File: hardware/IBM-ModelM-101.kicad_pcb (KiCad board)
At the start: 2 copper layers, 150 x 50 mm, 44 parts, among them J1 CONN-MOLEX-0670688000-USB-B, J2 KEYBOARD_ACTIVE_LINES, J3 KEYBOARD_INPUT_LINES, J4 CHASSIS_GROUND, J5 STATUS_LEDS, J6 DEBUG_FTDI, J7 JTAG, SW1 BOOT0, SW2 RESET, U1 TLV70233DBV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

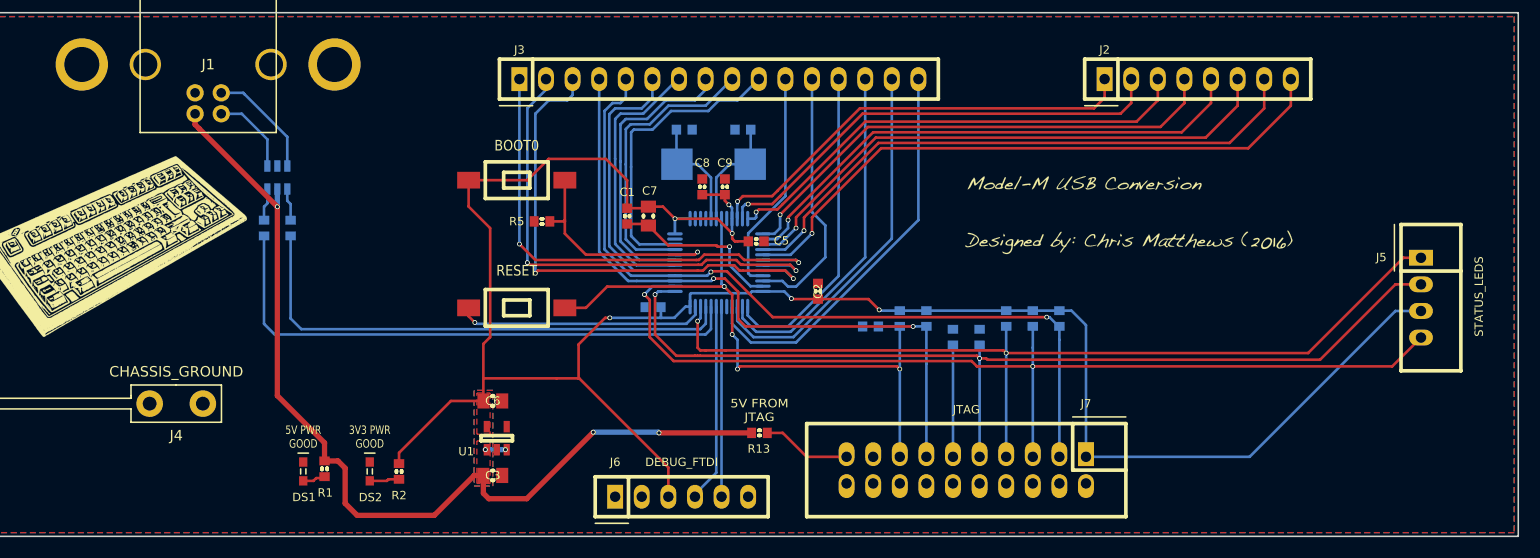
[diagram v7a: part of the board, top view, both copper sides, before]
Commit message: Final fixes to schematic and PCB layout
Fixed silk screen errors, added pin-out information to I/O headers and
JTAG.
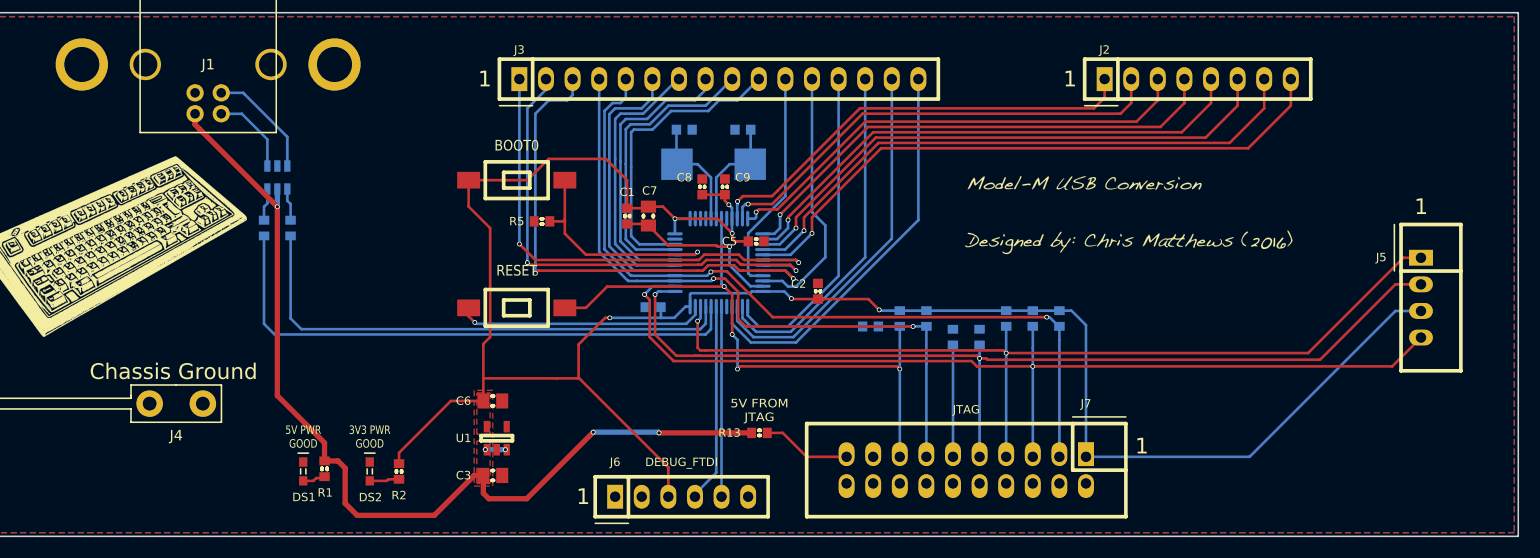
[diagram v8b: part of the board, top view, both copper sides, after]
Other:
- board text added: "1"
- board text added: "3V3"
- board text added: "5V"
- board text added: "Chassis Ground"
- board text added: "GND"
- board text added: "PA0"
- board text added: "PA1"
- board text added: "PA13/SWDIO"
- board text added: "PA14/SWCLK"
- board text added: "PA15/JTDI"
- board text added: "PA2"
- board text added: "PA3"
- board text added: "PA4"
- board text added: "PA5"
- board text added: "PA6"
- board text added: "PA7"
- board text added: "PB0"
- board text added: "PB1"
- board text added: "PB10"
- board text added: "PB11"
- board text added: "PB12"
- board text added: "PB13"
- board text added: "PB14"
- board text added: "PB15"
- board text added: "PB2"
- board text added: "PB3"
- board text added: "PB3/JTDO"
- board text added: "PB4"
- board text added: "PB4/JNTRST"
- board text added: "PB5"
- board text added: "PB6"
- board text added: "PB7"
- board text added: "PB8"
- board text added: "PB9"
- board text added: "RXD"
- board text added: "STM32F102C6"
- board text added: "TXD"
- board text added: "~RST~/~NRST"
